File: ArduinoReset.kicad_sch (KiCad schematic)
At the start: 2 parts

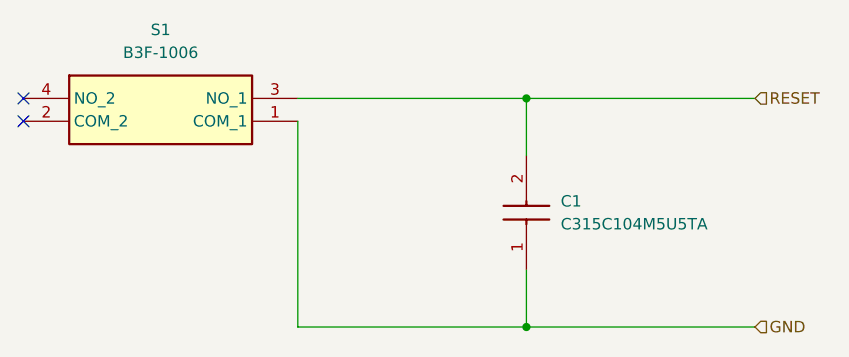
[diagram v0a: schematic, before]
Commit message: Swapped components for those in custom library, updated labelling on PCB.
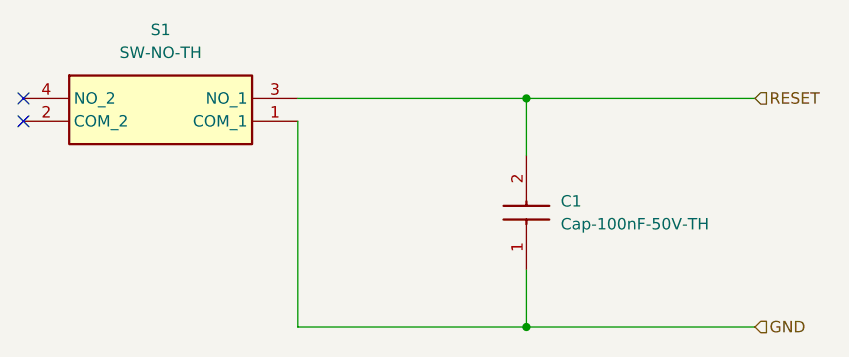
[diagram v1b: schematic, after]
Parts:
- C1: value C315C104M5U5TA -> Cap-100nF-50V-TH; footprint SamacSys_Parts:C315C100J2G5TA -> Custom:80-C315C104M5U; symbol SamacSys_Parts:C315C104M5U5TA -> Custom:Cap-100nF-50V-TH; Supplier (none) -> Mouser; Supplier Part Number (none) -> 80-C315C104M5U; Supplier Price/Stock (none) -> https://www.mouser.co.uk/ProductDetail/KEMET/C315C104M5U5TA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
- S1: value B3F-1006 -> SW-NO-TH; footprint SamacSys_Parts:B3F1006 -> Custom:653-B3F-1006; symbol SamacSys_Parts:B3F-1006 -> Custom:SW-NO-TH; Supplier (none) -> Mouser; Supplier Part Number (none) -> 653-B3F-1006; Supplier Price/Stock (none) -> https://www.mouser.co.uk/ProductDetail/Omron-Electronics/B3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
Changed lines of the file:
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@@
 	)
 	(symbol
-		(lib_id "SamacSys_Parts:C315C104M5U5TA")
+		(lib_id "Custom:Cap-100nF-50V-TH")
 		(at 165.1 107.95 90)
 		(unit 1)
@@
 			)
 		)
-		(property "Value" "C315C104M5U5TA"
+		(property "Value" "Cap-100nF-50V-TH"
 			(at 168.91 102.8699 90)
 			(effects
@@
 			)
 		)
-		(property "Footprint" "SamacSys_Parts:C315C100J2G5TA"
+		(property "Footprint" "Custom:80-C315C104M5U"
 			(at 261.29 99.06 0)
 			(effects
@@
 		(property "Manufacturer_Part_Number" "C315C104M5U5TA"
 			(at 961.29 99.06 0)
+			(effects
+				(font
+					(size 1.27 1.27)
+				)
+				(justify left top)
+				(hide yes)
+			)
+		)
+		(property "Supplier" "Mouser"
+			(at 165.1 107.95 0)
+			(effects
+				(font
+					(size 1.27 1.27)
+				)
+				(hide yes)
+			)
+		)
+		(property "Supplier Part Number" "80-C315C104M5U"
+			(at 661.29 99.06 0)
+			(effects
+				(font
+					(size 1.27 1.27)
+				)
+				(justify left top)
+				(hide yes)
+			)
+		)
+		(property "Supplier Price/Stock" "https://www.mouser.co.uk/ProductDetail/KEMET/C315C104M5U5TA?qs=yPUL72EuMSdlpklLgkTxlg%3D%3D"
+			(at 761.29 99.06 0)
 			(effects
 				(font
@@
 	)
 	(symbol
-		(lib_id "SamacSys_Parts:B3F-1006")
+		(lib_id "Custom:SW-NO-TH")
 		(at 109.22 88.9 0)
 		(unit 1)
@@
 			)
 		)
-		(property "Value" "B3F-1006"
+		(property "Value" "SW-NO-TH"
 			(at 124.46 83.82 0)
 			(effects
@@
 			)
 		)
-		(property "Footprint" "SamacSys_Parts:B3F1006"
+		(property "Footprint" "Custom:653-B3F-1006"
 			(at 135.89 183.82 0)
 			(effects
@@
 			)
 		)
-		(property "Description" "Tactile Switches Horizontal Flat 4.33 mm 4.9 N"
+		(property "Description" "Switch - Tactile Switches Horizontal Flat 4.33 mm 4.9 N"
 			(at 109.22 88.9 0)
 			(effects
@@
 			(effects
 				(font
+					(size 1.27 1.27)
+				)
+				(justify left top)
+				(hide yes)
+			)
+		)
+		(property "Supplier" "Mouser"
+			(at 109.22 88.9 0)
+			(effects
+				(font
+					(size 1.27 1.27)
+				)
+				(hide yes)
+			)
+		)
+		(property "Supplier Part Number" "653-B3F-1006"
+			(at 135.89 583.82 0)
+			(effects
+				(font
+					(size 1.27 1.27)
+				)
+				(justify left top)
+				(hide yes)
+			)
+		)
+		(property "Supplier Price/Stock" "https://www.mouser.co.uk/ProductDetail/Omron-Electronics/B3F-1006?qs=wE98CiVmOw78gCH%252BNiS1qg%3D%3D"
+			(at 135.89 683.82 0)
+			(effects
+				(font

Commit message: Updates look good, promoted to v1.2.
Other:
- title: Arduino Reset Circuit -> Arduino Mega CMRI WiFi Shield
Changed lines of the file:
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@@
 	(paper "A4")
 	(title_block
-		(title "Arduino Reset Circuit")
-		(date "2026-01-30")
-		(rev "1.1")
+		(title "Arduino Mega CMRI WiFi Shield")
+		(date "2026-02-10")
+		(rev "1.2")
 	)
 	(junction
